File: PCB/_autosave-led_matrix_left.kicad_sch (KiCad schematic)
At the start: 39 parts

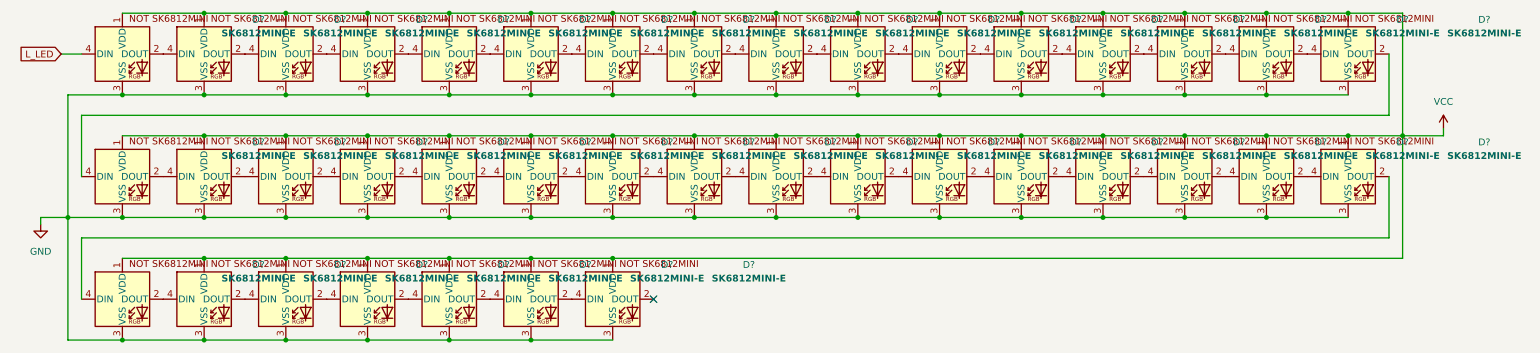
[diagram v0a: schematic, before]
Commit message: wired up leds and matrix for left
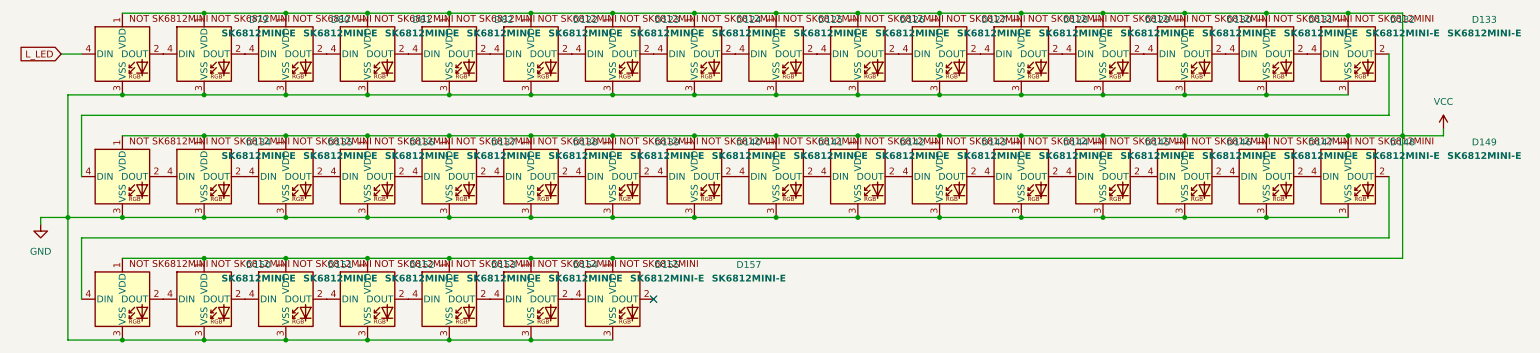
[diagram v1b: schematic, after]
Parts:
- gave numbers to parts that had none: 39
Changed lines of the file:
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@@
 		(dnp no)
 		(fields_autoplaced yes)
-		(property "Reference" "D?"
+		(property "Reference" "D152"
 			(at 90.17 64.6998 0)
 			(effects
@@
 		(dnp no)
 		(fields_autoplaced yes)
-		(property "Reference" "D?"
+		(property "Reference" "D79"
 			(at 59.69 18.9798 0)
 			(effects
@@
 		(dnp no)
 		(fields_autoplaced yes)
-		(property "Reference" "D?"
+		(property "Reference" "D81"
 			(at 90.17 18.9798 0)
 			(effects
@@
 		(dnp no)
 		(fields_autoplaced yes)
-		(property "Reference" "D?"
+		(property "Reference" "D144"
 			(at 212.09 41.8398 0)
 			(effects
@@
 		(dnp no)
 		(fields_autoplaced yes)
-		(property "Reference" "D?"
+		(property "Reference" "D143"
 			(at 196.85 41.8398 0)
 			(effects
@@
 		(dnp no)
 		(fields_autoplaced yes)
-		(property "Reference" "D?"
+		(property "Reference" "D128"
 			(at 212.09 18.9798 0)
 			(effects
@@
 		(dnp no)
 		(fields_autoplaced yes)
-		(property "Reference" "D?"
+		(property "Reference" "D127"
 			(at 196.85 18.9798 0)
 			(effects
@@
 		(dnp no)
 		(fields_autoplaced yes)
-		(property "Reference" "D?"
+		(property "Reference" "D130"
 			(at 242.57 18.9798 0)
 			(effects
@@
 		(dnp no)
 		(fields_autoplaced yes)
-		(property "Reference" "D?"
+		(property "Reference" "D142"
 			(at 181.61 41.8398 0)
 			(effects
@@
 		(dnp no)
 		(fields_autoplaced yes)
-		(property "Reference" "D?"
+		(property "Reference" "D123"
 			(at 135.89 18.9798 0)
 			(effects
@@
 		(dnp no)
 		(fields_autoplaced yes)
-		(property "Reference" "D?"
+		(property "Reference" "D135"
 			(at 74.93 41.8398 0)
 			(effects
@@
 		(dnp no)
 		(fields_autoplaced yes)
-		(property "Reference" "D?"
+		(property "Reference" "D131"
 			(at 257.81 18.9798 0)
 			(effects
@@
 		(dnp no)
 		(fields_autoplaced yes)
-		(property "Reference" "D?"
+		(property "Reference" "D151"
 			(at 74.93 64.6998 0)
 			(effects
@@
 		(dnp no)
 		(fields_autoplaced yes)
-		(property "Reference" "D?"
+		(property "Reference" "D138"
 			(at 120.65 41.8398 0)
 			(effects
@@
 		(dnp no)
 		(fields_autoplaced yes)
-		(property "Reference" "D?"
+		(property "Reference" "D124"
 			(at 151.13 18.9798 0)
 			(effects
@@
 		(dnp no)
 		(fields_autoplaced yes)
-		(property "Reference" "D?"
+		(property "Reference" "D136"
 			(at 90.17 41.8398 0)
 			(effects
@@
 		(dnp no)
 		(fields_autoplaced yes)
-		(property "Reference" "D?"
+		(property "Reference" "D154"
 			(at 120.65 64.6998 0)
 			(effects
@@
 		(dnp no)
 		(fields_autoplaced yes)
-		(property "Reference" "D?"
+		(property "Reference" "D134"
 			(at 59.69 41.8398 0)
 			(effects
@@
 		(dnp no)
 		(fields_autoplaced yes)
-		(property "Reference" "D?"
+		(property "Reference" "D145"
 			(at 227.33 41.8398 0)
 			(effects
@@
 		(dnp no)
 		(fields_autoplaced yes)
-		(property "Reference" "D?"
+		(property "Reference" "D157"
 			(at 151.13 64.6998 0)
 			(effects
@@
 		(dnp no)
 		(fields_autoplaced yes)
-		(property "Reference" "D?"
+		(property "Reference" "D133"
 			(at 288.29 18.9798 0)
 			(effects
@@
 		(dnp no)
 		(fields_autoplaced yes)
-		(property "Reference" "D?"
+		(property "Reference" "D137"
 			(at 105.41 41.8398 0)
 			(effects
@@
 		(dnp no)
 		(fields_autoplaced yes)
-		(property "Reference" "#PWR?"
+		(property "Reference" "#PWR011"
 			(at 19.05 63.5 0)
 			(effects
@@
 		(dnp no)
 		(fields_autoplaced yes)
-		(property "Reference" "D?"
+		(property "Reference" "D141"
 			(at 166.37 41.8398 0)
 			(effects
@@
 		(dnp no)
 		(fields_autoplaced yes)
-		(property "Reference" "D?"
+		(property "Reference" "D125"
 			(at 166.37 18.9798 0)
 			(effects
@@
 		(dnp no)
 		(fields_autoplaced yes)
-		(property "Reference" "D?"
+		(property "Reference" "D80"
 			(at 74.93 18.9798 0)
 			(effects
@@
 		(dnp no)
 		(fields_autoplaced yes)
-		(property "Reference" "#PWR?"
+		(property "Reference" "#PWR012"
 			(at 280.67 43.18 0)
 			(effects
@@
 		(dnp no)
 		(fields_autoplaced yes)
-		(property "Reference" "D?"
+		(property "Reference" "D150"
 			(at 59.69 64.6998 0)
 			(effects
@@
 		(dnp no)
 		(fields_autoplaced yes)
-		(property "Reference" "D?"
+		(property "Reference" "D148"
 			(at 273.05 41.8398 0)
 			(effects
@@
 		(dnp no)
 		(fields_autoplaced yes)
-		(property "Reference" "D?"
+		(property "Reference" "D155"
 			(at 135.89 64.6998 0)
 			(effects
@@
 		(dnp no)
 		(fields_autoplaced yes)
-		(property "Reference" "D?"
+		(property "Reference" "D146"
 			(at 242.57 41.8398 0)
 			(effects
@@
 		(dnp no)
 		(fields_autoplaced yes)
-		(property "Reference" "D?"
+		(property "Reference" "D140"
 			(at 151.13 41.8398 0)
 			(effects
@@
 		(dnp no)
 		(fields_autoplaced yes)
-		(property "Reference" "D?"
+		(property "Reference" "D149"
 			(at 288.29 41.8398 0)
 			(effects
@@
 		(dnp no)
 		(fields_autoplaced yes)
-		(property "Reference" "D?"
+		(property "Reference" "D147"
 			(at 257.81 41.8398 0)
 			(effects
@@
 		(dnp no)
 		(fields_autoplaced yes)
-		(property "Reference" "D?"
+		(property "Reference" "D132"
 			(at 273.05 18.9798 0)
 			(effects
@@
 		(dnp no)
 		(fields_autoplaced yes)
-		(property "Reference" "D?"
+		(property "Reference" "D153"
 			(at 105.41 64.6998 0)
 			(effects
@@
 		(dnp no)
 		(fields_autoplaced yes)
-		(property "Reference" "D?"
+		(property "Reference" "D126"
 			(at 181.61 18.9798 0)
 			(effects
@@
 		(dnp no)
 		(fields_autoplaced yes)
-		(property "Reference" "D?"
+		(property "Reference" "D122"
 			(at 120.65 18.9798 0)
 			(effects
@@
 		(dnp no)
 		(fields_autoplaced yes)
-		(property "Reference" "D?"
+		(property "Reference" "D139"
 			(at 135.89 41.8398 0)
 			(effects
@@
 		(dnp no)
 		(fields_autoplaced yes)
-		(property "Reference" "D?"
+		(property "Reference" "D129"
 			(at 227.33 18.9798 0)
 			(effects
@@
 		(dnp no)
 		(fields_autoplaced yes)
-		(property "Reference" "D?"
+		(property "Reference" "D82"
 			(at 105.41 18.9798 0)
 			(effects
